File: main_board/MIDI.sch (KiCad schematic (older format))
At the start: 13 parts

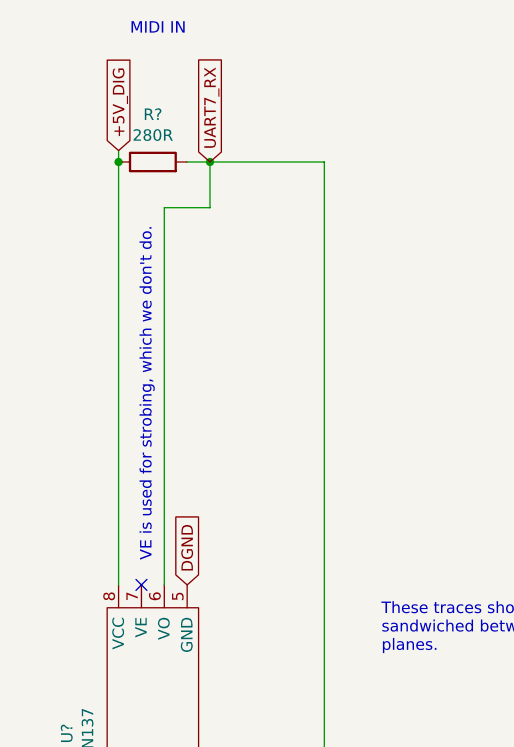
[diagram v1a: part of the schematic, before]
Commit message: Added MIDI connectors and SD card to io_board
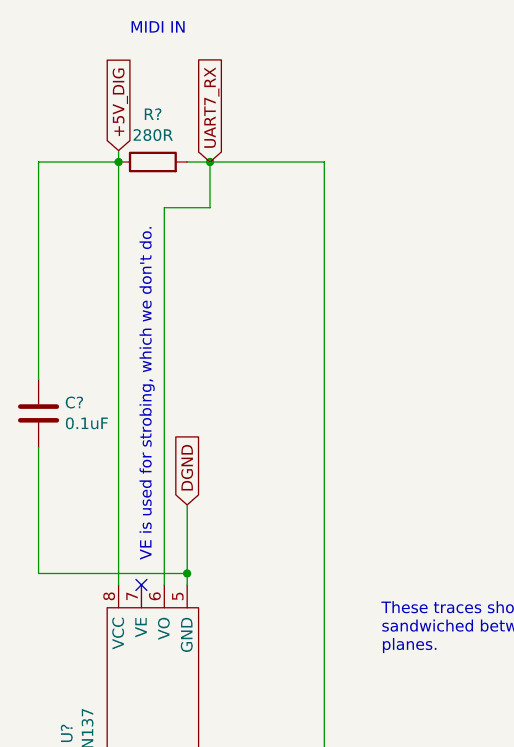
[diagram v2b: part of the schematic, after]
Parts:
- added C?: 0.1uF, symbol Device:C
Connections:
- net +5V_DIG: now also C?.1
- net DGND: now also C?.2
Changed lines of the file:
@@
 EESchema Schematic File Version 4
 LIBS:main_board-cache
-EELAYER 26 0
+EELAYER 29 0
 EELAYER END
 $Descr A4 11693 8268
 encoding utf-8
-Sheet 10 13
+Sheet 10 12
 Title ""
 Date ""
@@
 Wire Wire Line
 	1650 1250 2150 1250
-Text GLabel 1550 3100 1    50   Input ~ 0
+Text GLabel 1550 2750 1    50   Input ~ 0
 DGND
 Text GLabel 10250 5100 3    50   Input ~ 0
@@
 Wire Wire Line
 	4550 3300 4550 3200
+Wire Wire Line
+	1550 2750 1550 3050
+$Comp
+L Device:C C?
+U 1 1 5D437FB6
+P 900 2350
+F 0 "C?" H 1015 2396 50  0000 L CNN
+F 1 "0.1uF" H 1015 2305 50  0000 L CNN
+F 2 "" H 938 2200 50  0001 C CNN
+F 3 "~" H 900 2350 50  0001 C CNN
+	1    900  2350
+	1    0    0    -1
+$EndComp
+Wire Wire Line
+	1250 1250 900  1250
+Wire Wire Line
+	900  1250 900  2200
+Wire Wire Line
+	900  2500 900  3050
+Wire Wire Line
+	900  3050 1550 3050
+Connection ~ 1550 3050
+Wire Wire Line
+	1550 3050 1550 3100
 $EndSCHEMATC
